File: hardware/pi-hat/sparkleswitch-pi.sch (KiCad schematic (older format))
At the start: 22 parts, among them J1 Conn_01x02, J2 Conn_02x06_Odd_Even, P1 CONN_02X20, U1 74HCT245, U2 74HCT245, U3 74HCT245, U4 PC817, U5 PC817, U6 PC817, U7 PC817

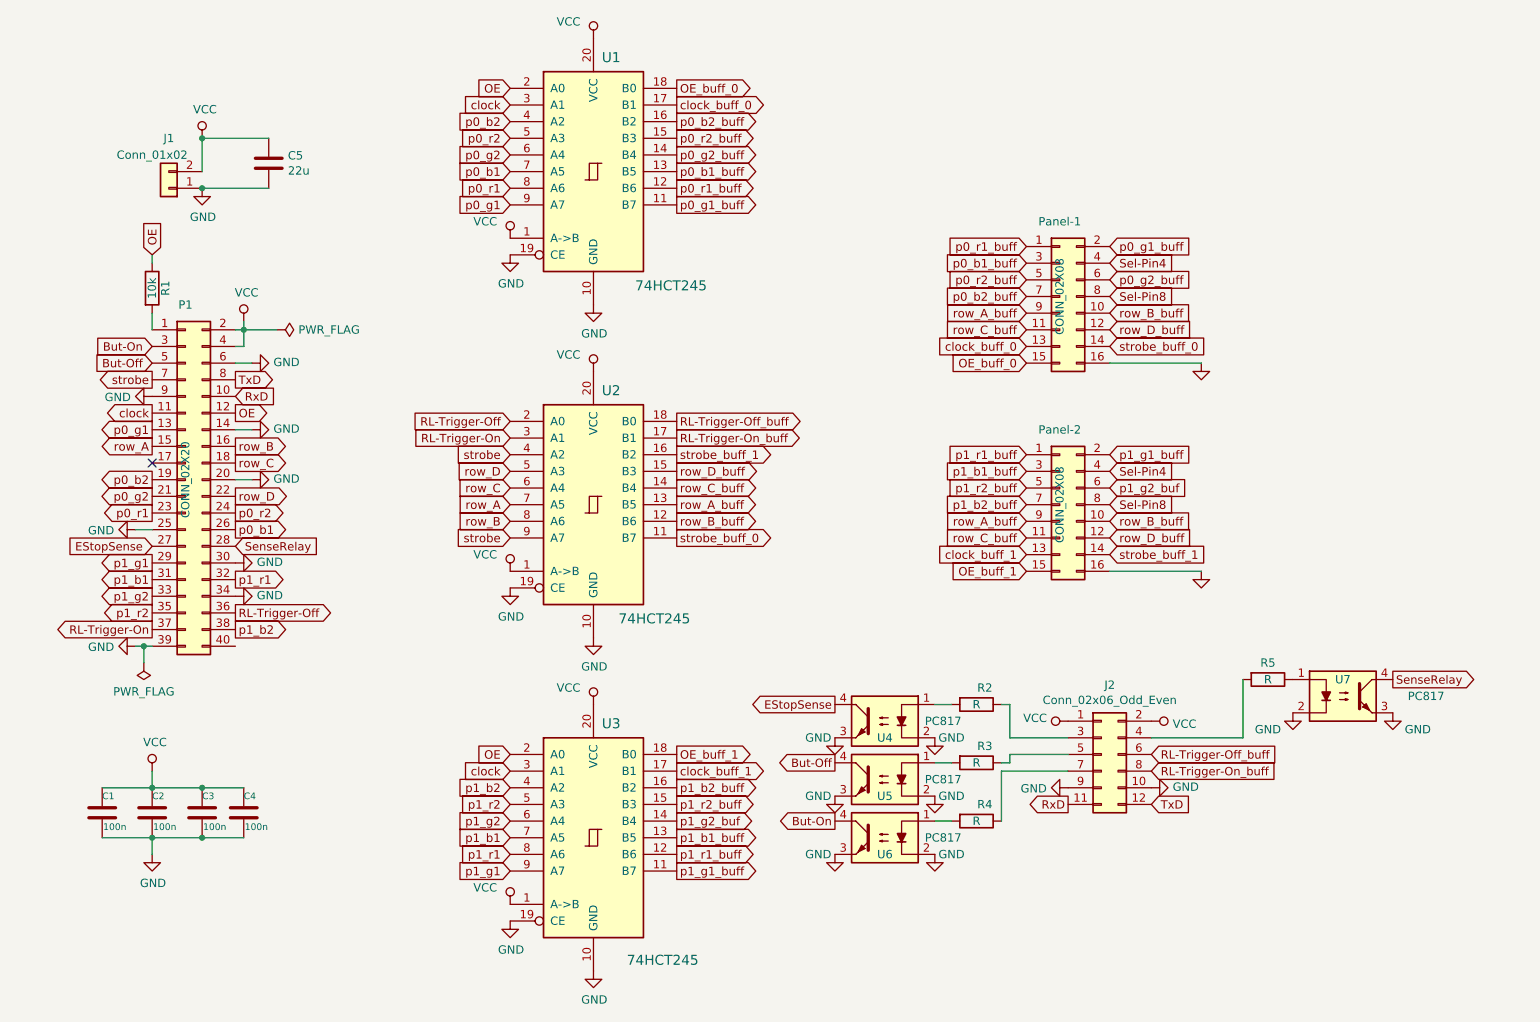
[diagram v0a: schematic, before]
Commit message: First wiring up with somewhat minimized via count.
This required to rewire GPIOs a little, but since this is a specific
set-up anyway.
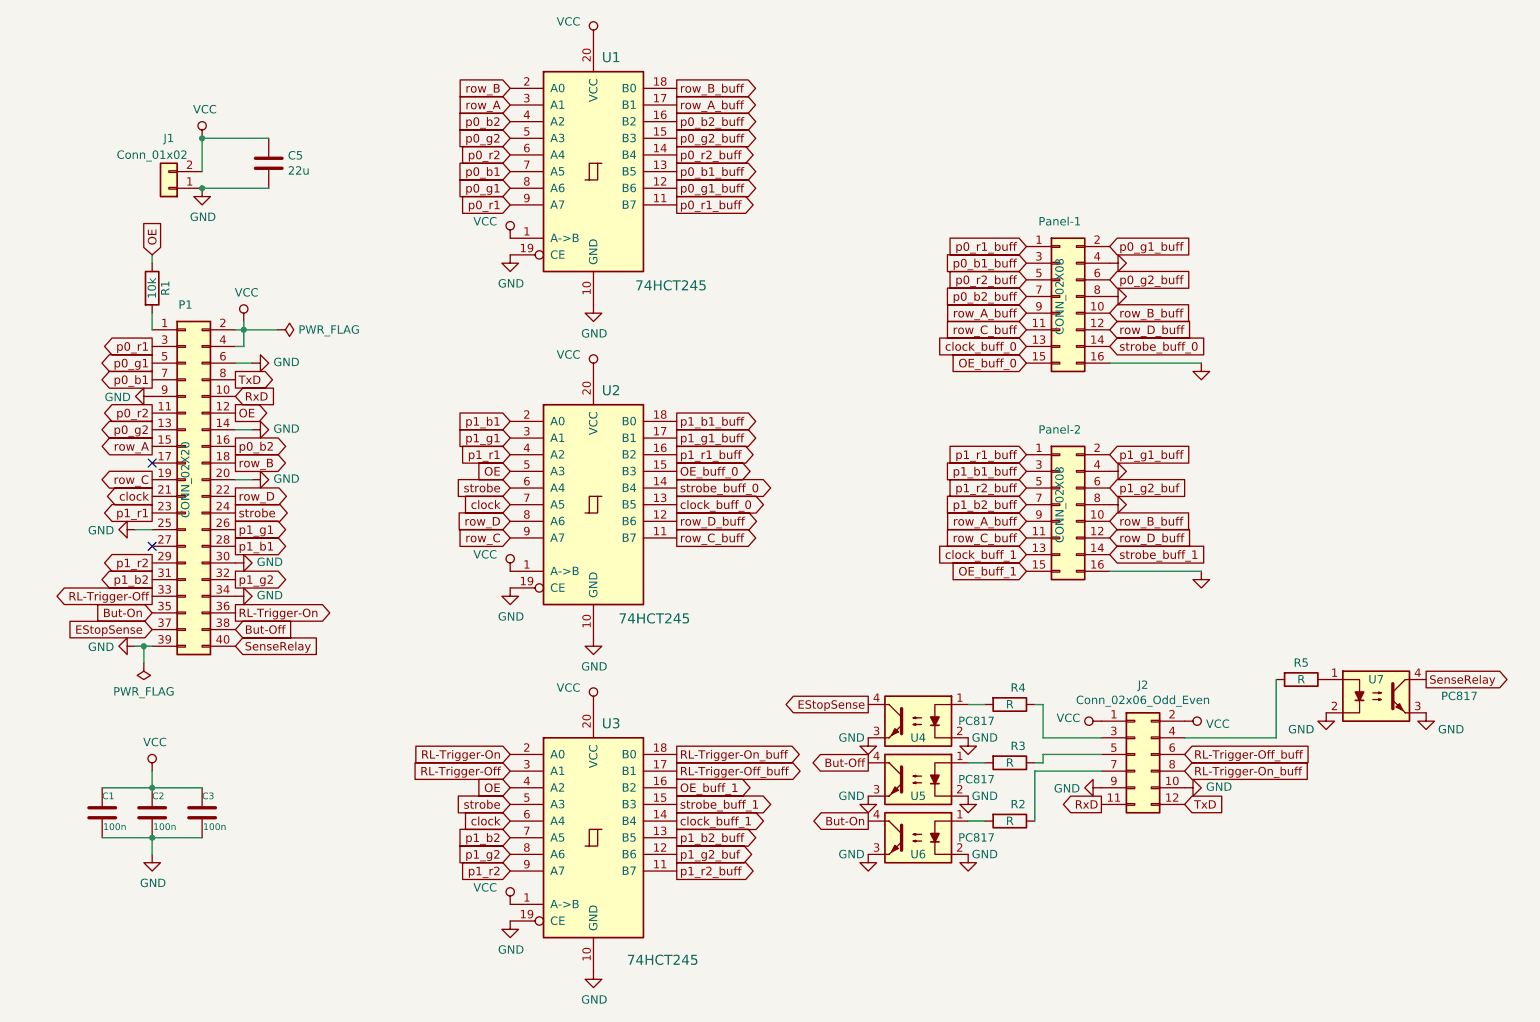
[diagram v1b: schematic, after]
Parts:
- removed C4: 100n, Capacitors_SMD:C_0805_HandSoldering, symbol device:C
- C1, C2, C3: footprint Capacitors_SMD:C_0805_HandSoldering -> Capacitors_SMD:C_0603
- renumbered R4 to R2, R2 to R4
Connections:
- net Sel-Pin4 is gone; now on net GND: Panel-1.4 (Pin_4), Panel-2.4 (Pin_4)
- net Sel-Pin8 is gone; now on net GND: Panel-1.8 (Pin_8), Panel-2.8 (Pin_8)
- net But-Off: now also P1.38 (Pin_38); no longer P1.5 (Pin_5)
- net But-On: now also P1.35 (Pin_35); no longer P1.3 (Pin_3)
- net EStopSense: now also P1.37 (Pin_37); no longer P1.27 (Pin_27)
- net OE: now also U2.5 (A3), U3.4 (A2); no longer U1.2 (A0), U3.2 (A0)
- net OE_buff_0: now also U2.15 (B3); no longer U1.18 (B0)
- net OE_buff_1: now also U3.16 (B2); no longer U3.18 (B0)
- net RL-Trigger-Off: now also P1.33 (Pin_33), U3.3 (A1); no longer P1.36 (Pin_36), U2.2 (A0)
- net RL-Trigger-Off_buff: now also U3.17 (B1); no longer U2.18 (B0)
- net RL-Trigger-On: now also P1.36 (Pin_36), U3.2 (A0); no longer P1.37 (Pin_37), U2.3 (A1)
- net RL-Trigger-On_buff: now also U3.18 (B0); no longer U2.17 (B1)
- net SenseRelay: now also P1.40 (Pin_40); no longer P1.28 (Pin_28)
- net clock: now also P1.21 (Pin_21), U2.7 (A5), U3.6 (A4); no longer P1.11 (Pin_11), U1.3 (A1), U3.3 (A1)
- net clock_buff_0: now also U2.13 (B5); no longer U1.17 (B1)
- net clock_buff_1: now also U3.14 (B4); no longer U3.17 (B1)
- net p0_b1: now also P1.7 (Pin_7); no longer P1.26 (Pin_26)
- net p0_b2: now also P1.16 (Pin_16); no longer P1.19 (Pin_19)
- net p0_g1: now also P1.5 (Pin_5), U1.8 (A6); no longer P1.13 (Pin_13), U1.9 (A7)
- net p0_g1_buff: now also U1.12 (B6); no longer U1.11 (B7)
- net p0_g2: now also P1.13 (Pin_13), U1.5 (A3); no longer P1.21 (Pin_21), U1.6 (A4)
- net p0_g2_buff: now also U1.15 (B3); no longer U1.14 (B4)
- net p0_r1: now also P1.3 (Pin_3), U1.9 (A7); no longer P1.23 (Pin_23), U1.8 (A6)
- net p0_r1_buff: now also U1.11 (B7); no longer U1.12 (B6)
- net p0_r2: now also P1.11 (Pin_11), U1.6 (A4); no longer P1.24 (Pin_24), U1.5 (A3)
- net p0_r2_buff: now also U1.14 (B4); no longer U1.15 (B3)
- net p1_b1: now also P1.28 (Pin_28), U2.2 (A0); no longer P1.31 (Pin_31), U3.7 (A5)
- net p1_b1_buff: now also U2.18 (B0); no longer U3.13 (B5)
- net p1_b2: now also P1.31 (Pin_31), U3.7 (A5); no longer P1.38 (Pin_38), U3.4 (A2)
- net p1_b2_buff: now also U3.13 (B5); no longer U3.16 (B2)
- net p1_g1: now also P1.26 (Pin_26), U2.3 (A1); no longer P1.29 (Pin_29), U3.9 (A7)
- net p1_g1_buff: now also U2.17 (B1); no longer U3.11 (B7)
- net p1_g2: now also P1.32 (Pin_32), U3.8 (A6); no longer P1.33 (Pin_33), U3.6 (A4)
- net p1_g2_buf: now also U3.12 (B6); no longer U3.14 (B4)
- net p1_r1: now also P1.23 (Pin_23), U2.4 (A2); no longer P1.32 (Pin_32), U3.8 (A6)
- net p1_r1_buff: now also U2.16 (B2); no longer U3.12 (B6)
- net p1_r2: now also P1.29 (Pin_29), U3.9 (A7); no longer P1.35 (Pin_35), U3.5 (A3)
- net p1_r2_buff: now also U3.11 (B7); no longer U3.15 (B3)
- net row_A: now also U1.3 (A1); no longer U2.7 (A5)
- net row_A_buff: now also U1.17 (B1); no longer U2.13 (B5)
- net row_B: now also P1.18 (Pin_18), U1.2 (A0); no longer P1.16 (Pin_16), U2.8 (A6)
- net row_B_buff: now also U1.18 (B0); no longer U2.12 (B6)
- net row_C: now also P1.19 (Pin_19), U2.9 (A7); no longer P1.18 (Pin_18), U2.6 (A4)
- net row_C_buff: now also U2.11 (B7); no longer U2.14 (B4)
- net row_D: now also U2.8 (A6); no longer U2.5 (A3)
- net row_D_buff: now also U2.12 (B6); no longer U2.15 (B3)
- net strobe: now also P1.24 (Pin_24), U2.6 (A4), U3.5 (A3); no longer P1.7 (Pin_7), U2.4 (A2), U2.9 (A7)
- net strobe_buff_0: now also U2.14 (B4); no longer U2.11 (B7)
- net strobe_buff_1: now also U3.15 (B3); no longer U2.16 (B2)
- no-connect marks 1 -> 2
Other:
- moved on the sheet: J2, R2, R3, R4, R5, U4, U5, U6, U7

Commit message: Make traces thicker as we have the space.
o Increase size of traces from 0.25mm to 0.4mm as space is
  not that constricted (right now only the afferent traces).
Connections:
- net GND: no longer P1.9 (Pin_9)
- no-connect marks 2 -> 3
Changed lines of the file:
@@
 	0    -1   -1   0
-$EndComp
-$Comp
-L power:GND #PWR0114
-U 1 1 5BD3AA48
-P 3000 3100
-F 0 "#PWR0114" H 3000 2850 50  0001 C CNN
-F 1 "GND" V 3005 2972 50  0000 R CNN
-F 2 "" H 3000 3100 50  0001 C CNN
-F 3 "" H 3000 3100 50  0001 C CNN
-	1    3000 3100
-	0    1    1    0
 $EndComp
 Text GLabel 7300 5300 0    50   Output ~ 0
@@
 	0    -1   -1   0
 $EndComp
+NoConn ~ 3000 3100
 $EndSCHEMATC

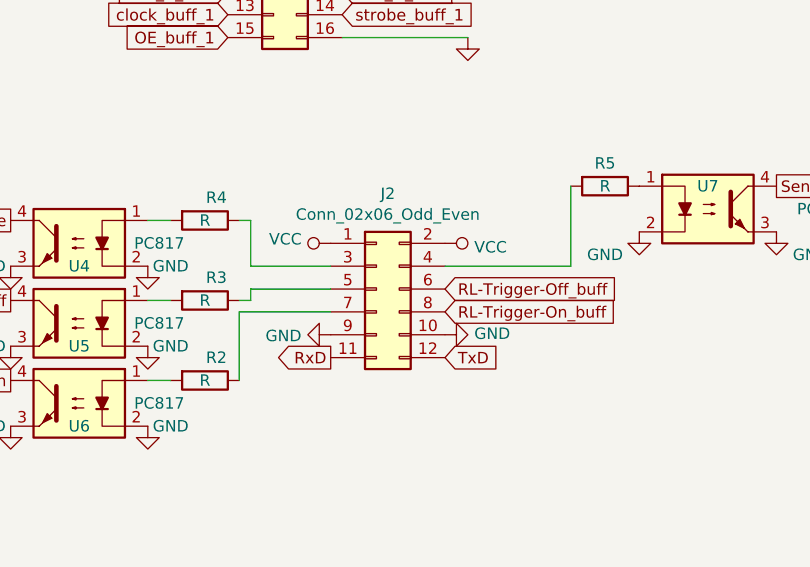
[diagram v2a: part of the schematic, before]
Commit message: Center middle '245
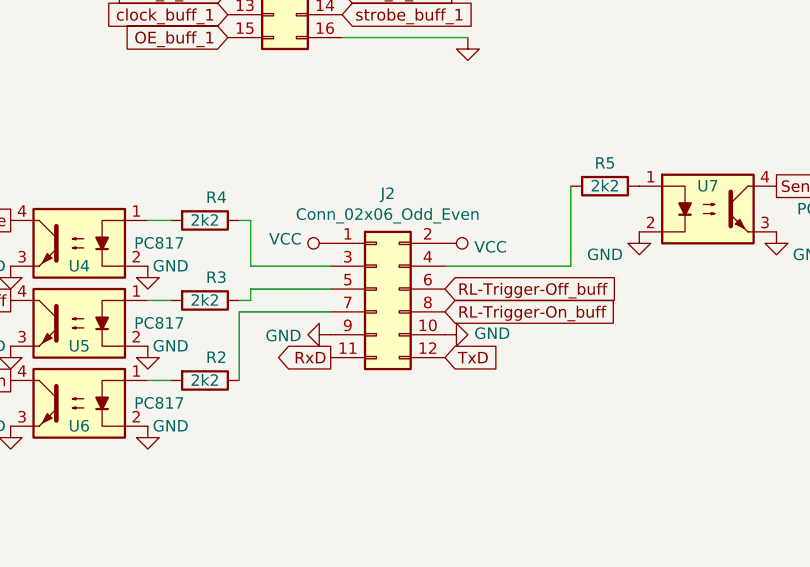
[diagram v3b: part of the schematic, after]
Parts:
- R2, R3, R4, R5: value R -> 2k2
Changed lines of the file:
@@
 P 9900 4800
 F 0 "R5" V 9800 4800 50  0000 C CNN
-F 1 "R" V 9900 4800 50  0000 C CNN
+F 1 "2k2" V 9900 4800 50  0000 C CNN
 F 2 "Resistors_SMD:R_0603" V 9830 4800 50  0001 C CNN
 F 3 "" H 9900 4800 50  0001 C CNN
@@
 P 8150 4950
 F 0 "R4" V 8050 5000 50  0000 C CNN
-F 1 "R" V 8150 4950 50  0000 C CNN
+F 1 "2k2" V 8150 4950 50  0000 C CNN
 F 2 "Resistors_SMD:R_0603" V 8080 4950 50  0001 C CNN
 F 3 "" H 8150 4950 50  0001 C CNN
@@
 P 8150 5300
 F 0 "R3" V 8050 5350 50  0000 C CNN
-F 1 "R" V 8150 5300 50  0000 C CNN
+F 1 "2k2" V 8150 5300 50  0000 C CNN
 F 2 "Resistors_SMD:R_0603" V 8080 5300 50  0001 C CNN
 F 3 "" H 8150 5300 50  0001 C CNN
@@
 P 8150 5650
 F 0 "R2" V 8050 5700 50  0000 C CNN
-F 1 "R" V 8150 5650 50  0000 C CNN
+F 1 "2k2" V 8150 5650 50  0000 C CNN
 F 2 "Resistors_SMD:R_0603" V 8080 5650 50  0001 C CNN
 F 3 "" H 8150 5650 50  0001 C CNN

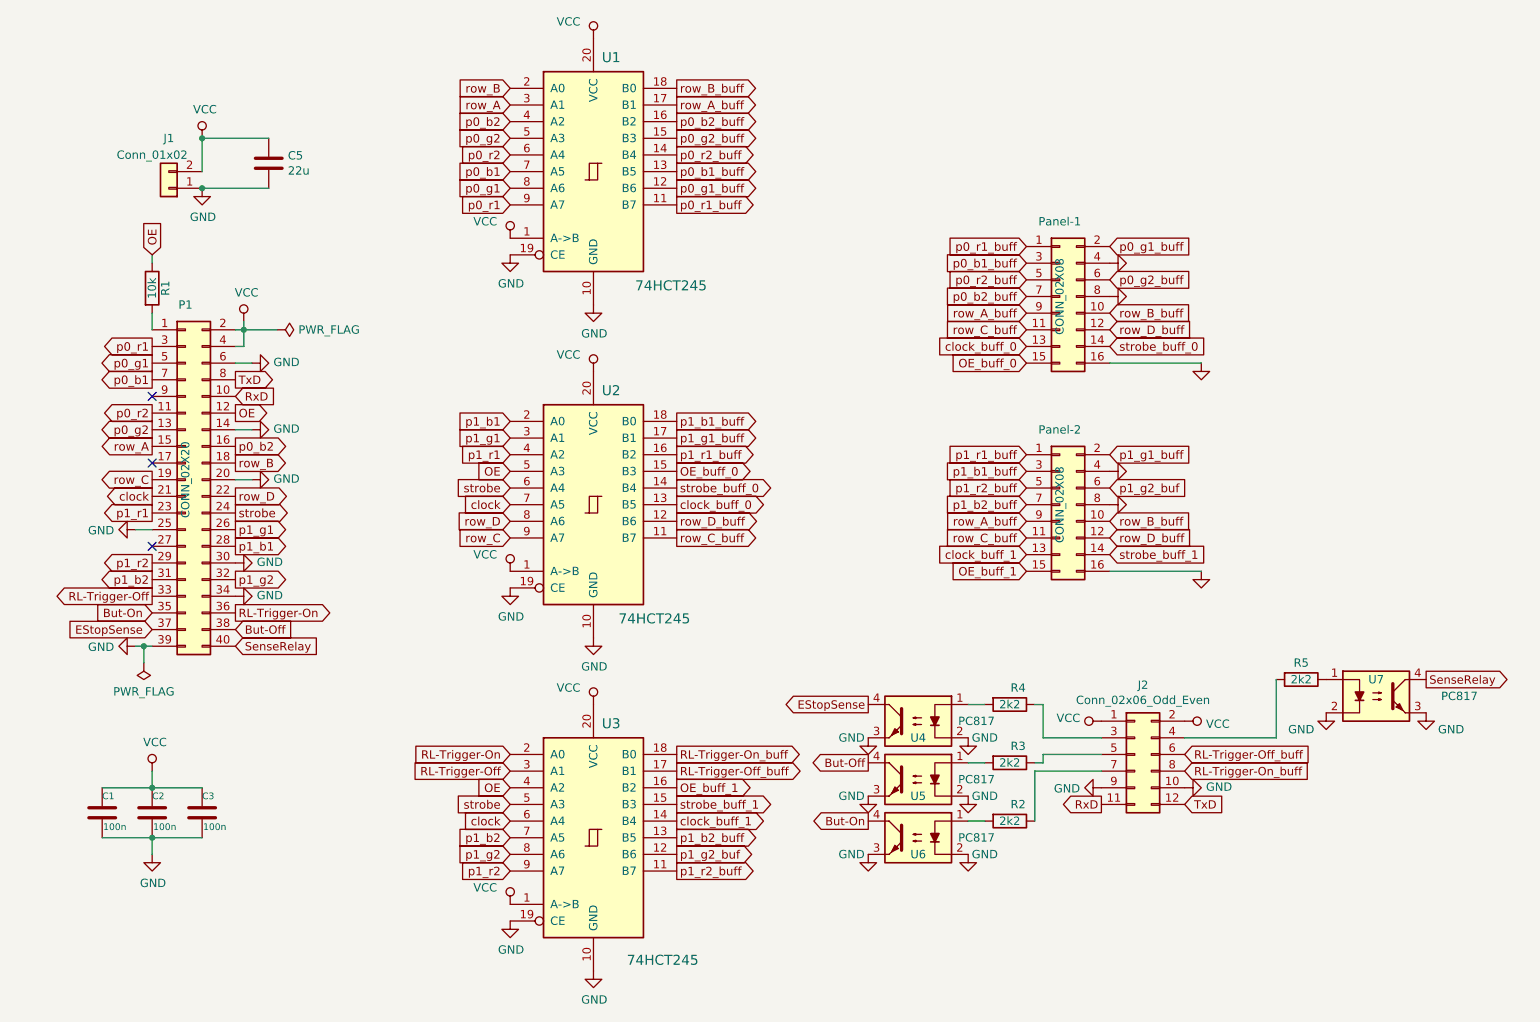
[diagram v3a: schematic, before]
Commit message: Add helpful silkscreen markings.
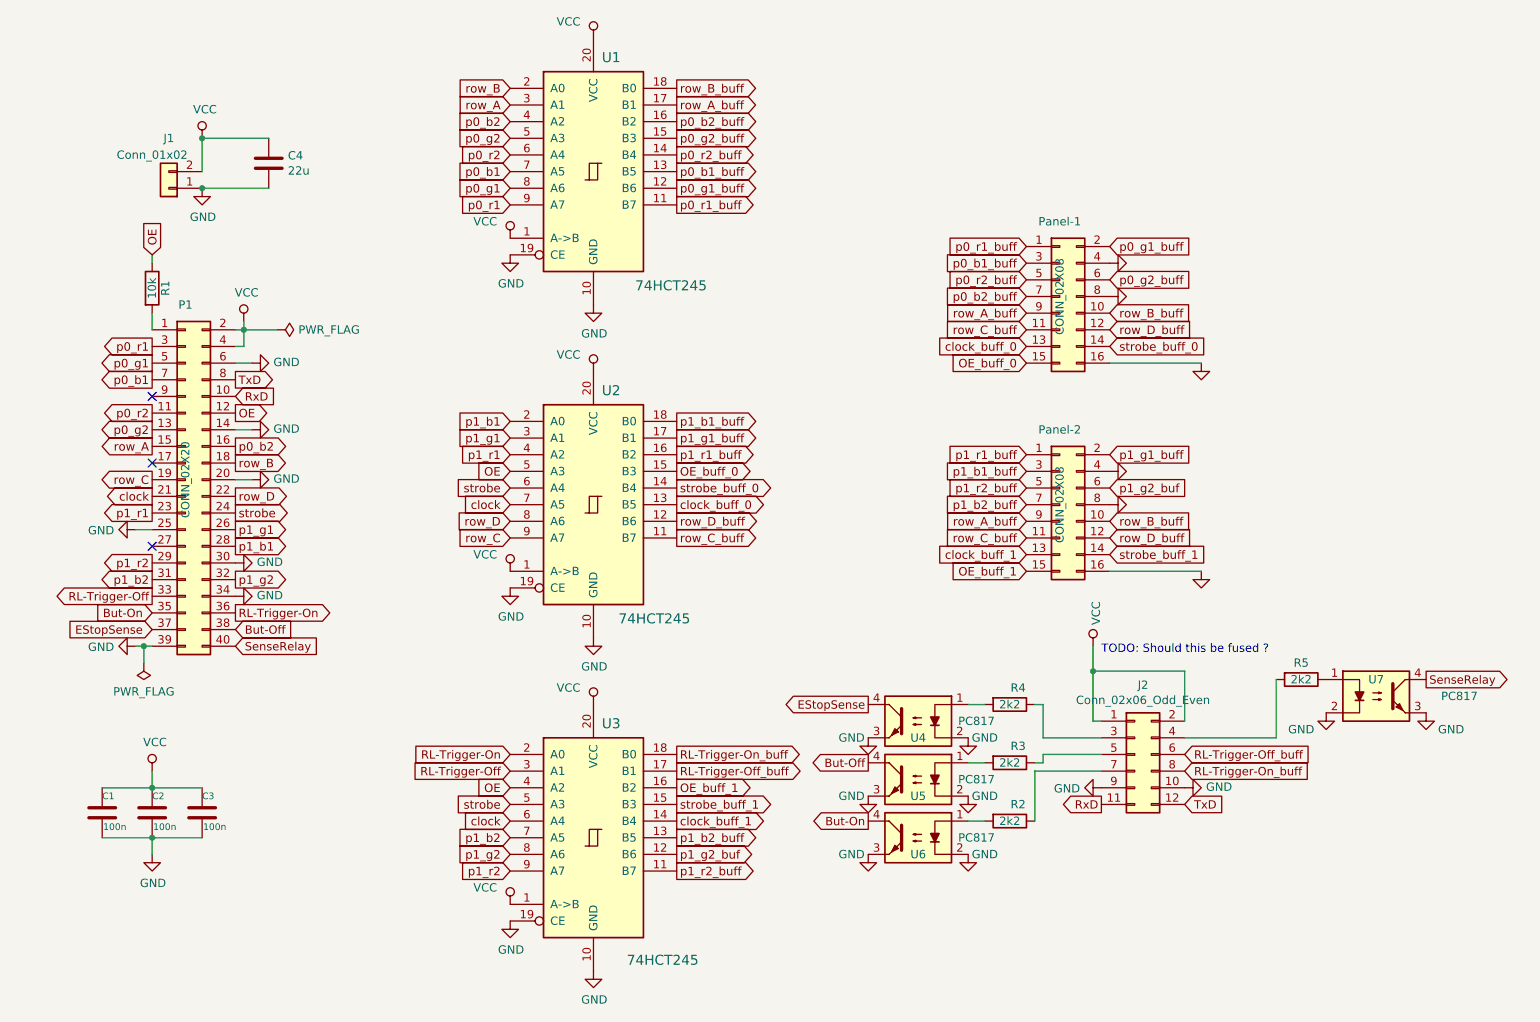
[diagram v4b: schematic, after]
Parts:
- renumbered C5 to C4
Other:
- note added: "TODO: Should this be fused ?"
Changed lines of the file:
@@
 $EndComp
 $Comp
-L device:C C5
+L device:C C4
 U 1 1 5BD19FEF
 P 3700 1700
-F 0 "C5" H 3815 1746 50  0000 L CNN
+F 0 "C4" H 3815 1746 50  0000 L CNN
 F 1 "22u" H 3815 1655 50  0000 L CNN
 F 2 "Capacitors_SMD:C_1210" H 3738 1550 50  0001 C CNN
@@
 $EndComp
 $Comp
-L power:VCC #PWR0101
-U 1 1 5BD25E1A
-P 9200 5050
-F 0 "#PWR0101" H 9200 4900 50  0001 C CNN
-F 1 "VCC" V 9217 5178 50  0000 L CNN
-F 2 "" H 9200 5050 50  0001 C CNN
-F 3 "" H 9200 5050 50  0001 C CNN
-	1    9200 5050
-	0    1    1    0
-$EndComp
-$Comp
 L power:VCC #PWR0102
 U 1 1 5BD264A0
-P 8700 5050
-F 0 "#PWR0102" H 8700 4900 50  0001 C CNN
-F 1 "VCC" V 8718 5177 50  0000 L CNN
-F 2 "" H 8700 5050 50  0001 C CNN
-F 3 "" H 8700 5050 50  0001 C CNN
-	1    8700 5050
-	0    -1   -1   0
+P 8650 4600
+F 0 "#PWR0102" H 8650 4450 50  0001 C CNN
+F 1 "VCC" V 8668 4727 50  0000 L CNN
+F 2 "" H 8650 4600 50  0001 C CNN
+F 3 "" H 8650 4600 50  0001 C CNN
+	1    8650 4600
+	1    0    0    -1
 $EndComp
 $Comp
@@
 $EndComp
 NoConn ~ 3000 3100
+Wire Wire Line
+	8650 4600 8650 4750
+Wire Wire Line
+	8650 5050 8700 5050
+Wire Wire Line
+	8650 4750 9200 4750
+Wire Wire Line
+	9200 4750 9200 5050
+Connection ~ 8650 4750
+Wire Wire Line
+	8650 4750 8650 5050
+Text Notes 8700 4650 0    50   ~ 0
+TODO: Should this be fused ?
 $EndSCHEMATC
